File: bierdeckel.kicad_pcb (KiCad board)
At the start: 2 copper layers, 93 x 93 mm, 58 parts, among them J1 Pogo, J2 Pogo, J3 Pogo, J4 Pogo, SW1 Address Coding, SW2 PTS526 SK15 SMTR2 LFS, SW3 PTS526 SK15 SMTR2 LFS, U1 ESP32-C3-WROOM-02, U2 BQ25176J, U3 TPS61201DRC, U4 TLV9101IDBVR

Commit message: update design
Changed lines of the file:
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@@
 		(polygon
 			(pts
-				(xy 143.34 96.357499) (xy 139.34 96.357499) (xy 138.09 96.357499) (xy 138.09 92.957499) (xy 143.34 92.9575)
+				(xy 143.345172 95.880061) (xy 139.186213 95.889824) (xy 139.093466 96.358439) (xy 138.09 96.357499)
+				(xy 138.09 92.957499) (xy 143.34 92.9575)
 			)
 		)

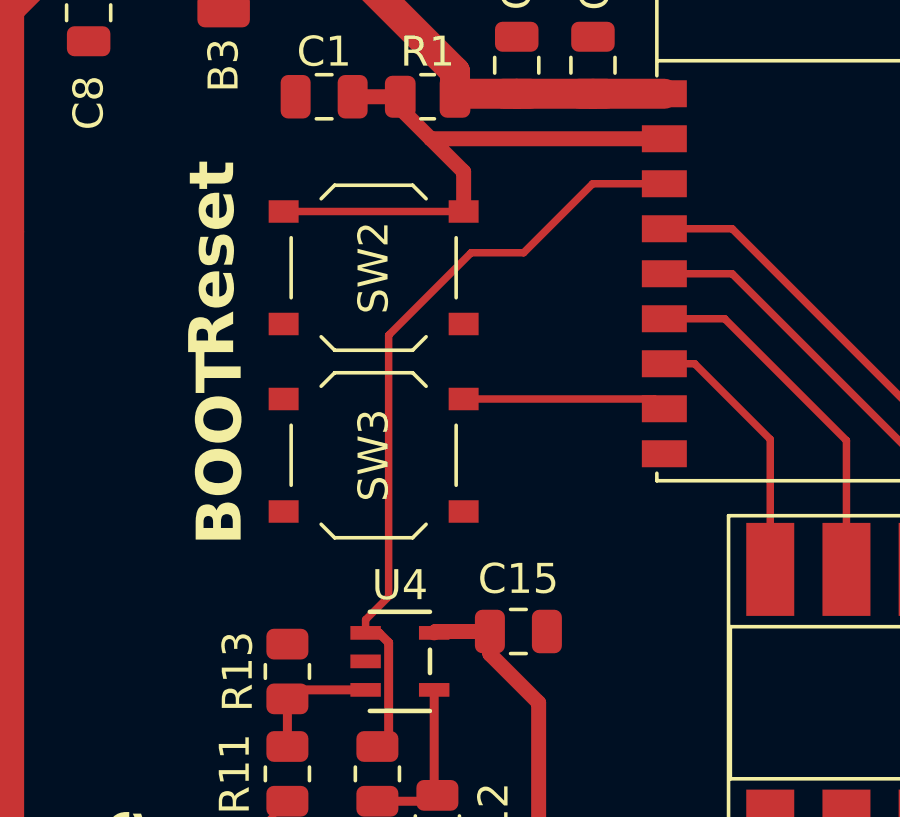
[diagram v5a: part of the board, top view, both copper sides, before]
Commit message: fix ERC
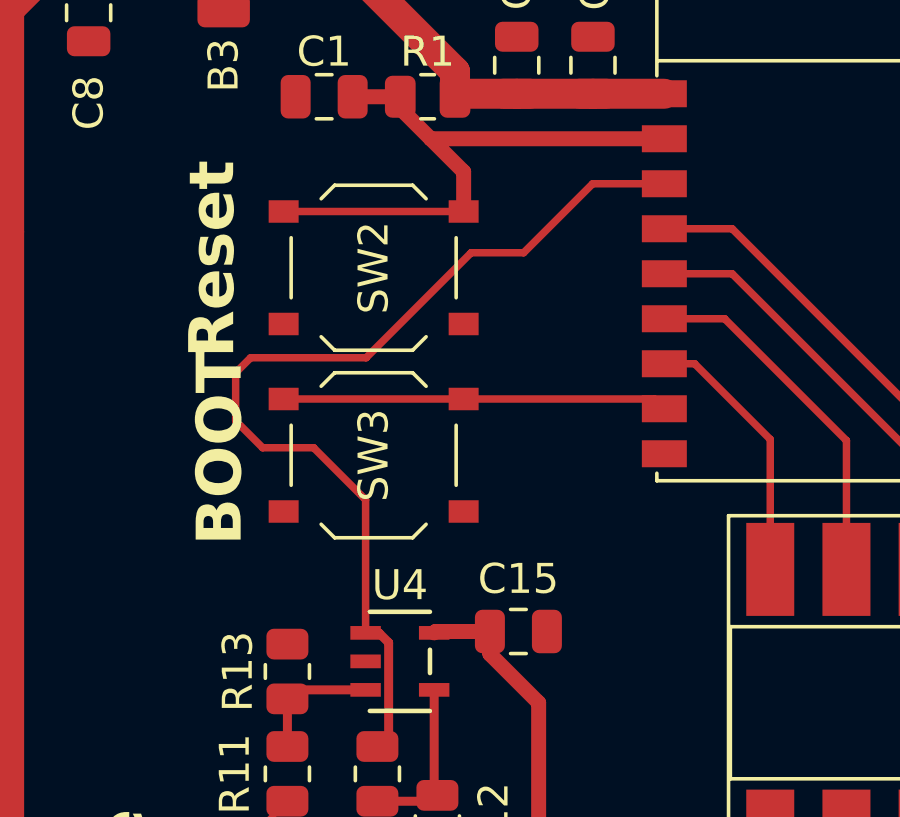
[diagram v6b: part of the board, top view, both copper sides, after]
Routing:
- net /Vpress: track 26.0 -> 32.9 mm
- net /~{BOOTLOADER}: track 6.82 -> 12.8 mm
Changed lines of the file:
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@@
 	)
 	(segment
-		(start 123.5 69.5)
+		(start 128.19 67.2)
 		(end 125.8 67.2)
 		(width 0.25)
@@
 	(segment
 		(start 121.75 69.5)
-		(end 123.5 69.5)
-		(width 0.25)
-		(layer "F.Cu")
-		(net 14)
-	)
-	(segment
-		(start 118.232002 82.170691)
-		(end 118.232002 81.732002)
+		(end 118.25 73)
+		(width 0.25)
+		(layer "F.Cu")
+		(net 14)
+	)
+	(segment
+		(start 113.9 75.1)
+		(end 114.8 76)
+		(width 0.25)
+		(layer "F.Cu")
+		(net 14)
+	)
+	(segment
+		(start 116.5 76)
+		(end 118.232002 77.732002)
+		(width 0.25)
+		(layer "F.Cu")
+		(net 14)
+	)
+	(segment
+		(start 118.25 73)
+		(end 114.4 73)
+		(width 0.25)
+		(layer "F.Cu")
+		(net 14)
+	)
+	(segment
+		(start 114.8 76)
+		(end 116.5 76)
 		(width 0.25)
 		(layer "F.Cu")
@@
 	)
 	(segment
-		(start 119 80.964004)
-		(end 119 72.25)
+		(start 113.9 73.5)
+		(end 113.9 75.1)
 		(width 0.25)
 		(layer "F.Cu")
@@
 	)
 	(segment
+		(start 123.5 69.5)
+		(end 121.75 69.5)
+		(width 0.25)
+		(layer "F.Cu")
+		(net 14)
+	)
+	(segment
 		(start 119 85.583193)
 		(end 119 82.495691)
@@
 	)
 	(segment
-		(start 119 72.25)
-		(end 121.75 69.5)
+		(start 114.4 73)
+		(end 113.9 73.5)
 		(width 0.25)
 		(layer "F.Cu")
@@
 	(segment
 		(start 125.8 67.2)
-		(end 128.19 67.2)
-		(width 0.25)
-		(layer "F.Cu")
-		(net 14)
-	)
-	(segment
-		(start 118.232002 81.732002)
-		(end 119 80.964004)
+		(end 123.5 69.5)
+		(width 0.25)
+		(layer "F.Cu")
+		(net 14)
+	)
+	(segment
+		(start 118.232002 77.732002)
+		(end 118.232002 82.170691)
 		(width 0.25)
 		(layer "F.Cu")
@@
 		(width 0.25)
 		(layer "F.Cu")
+		(net 39)
+	)
+	(segment
+		(start 115.5 74.375)
+		(end 121.5 74.375)
+		(width 0.25)
+		(layer "F.Cu")
